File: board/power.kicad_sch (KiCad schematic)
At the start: 22 parts, among them Q1 BSS138, Q2 BSS138, Q3 BSS138, U1 OKI-78SR-5_1.5-W36H-C

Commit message: assigned footprints
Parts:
- C1, C2: footprint (none) -> Capacitor_SMD:C_0603_1608Metric_Pad1.08x0.95mm_HandSolder
- Conn1, Conn11, Conn14, Conn15: footprint (none) -> MRDT_Connectors:Square_Anderson_2_H_Side_By_Side_PV
- D1, D2, D3, D4, D5, D6: footprint (none) -> LED_SMD:LED_0603_1608Metric_Pad1.05x0.95mm_HandSolder
- R1, R2, R3, R6, R7, R8: footprint (none) -> Resistor_SMD:R_0603_1608Metric_Pad0.98x0.95mm_HandSolder
- U1: footprint Converter_DCDC:Converter_DCDC_Murata_OKI-78SR_Horizontal -> MRDT_Devices:OKI_Horizontal
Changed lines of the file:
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@@
 			)
 		)
-		(property "Footprint" ""
+		(property "Footprint" "LED_SMD:LED_0603_1608Metric_Pad1.05x0.95mm_HandSolder"
 			(at 87.63 100.33 0)
 			(effects
@@
 			)
 		)
-		(property "Footprint" ""
+		(property "Footprint" "LED_SMD:LED_0603_1608Metric_Pad1.05x0.95mm_HandSolder"
 			(at 168.91 48.26 0)
 			(effects
@@
 			)
 		)
-		(property "Footprint" ""
+		(property "Footprint" "Capacitor_SMD:C_0603_1608Metric_Pad1.08x0.95mm_HandSolder"
 			(at 93.6752 49.53 0)
 			(effects
@@
 			)
 		)
-		(property "Footprint" ""
+		(property "Footprint" "MRDT_Connectors:Square_Anderson_2_H_Side_By_Side_PV"
 			(at 26.67 114.3 0)
 			(effects
@@
 			)
 		)
-		(property "Footprint" ""
+		(property "Footprint" "MRDT_Connectors:Square_Anderson_2_H_Side_By_Side_PV"
 			(at 25.4 60.96 0)
 			(effects
@@
 			)
 		)
-		(property "Footprint" "Converter_DCDC:Converter_DCDC_Murata_OKI-78SR_Horizontal"
+		(property "Footprint" "MRDT_Devices:OKI_Horizontal"
 			(at 109.22 45.72 0)
 			(effects
@@
 			)
 		)
-		(property "Footprint" ""
+		(property "Footprint" "MRDT_Connectors:Square_Anderson_2_H_Side_By_Side_PV"
 			(at 26.67 201.93 0)
 			(effects
@@
 			)
 		)
-		(property "Footprint" ""
+		(property "Footprint" "MRDT_Connectors:Square_Anderson_2_H_Side_By_Side_PV"
 			(at 25.4 49.53 0)
 			(effects
@@
 			)
 		)
-		(property "Footprint" ""
+		(property "Footprint" "MRDT_Connectors:Square_Anderson_2_H_Side_By_Side_PV"
 			(at 26.67 143.51 0)
 			(effects
@@
 			)
 		)
-		(property "Footprint" ""
+		(property "Footprint" "LED_SMD:LED_0603_1608Metric_Pad1.05x0.95mm_HandSolder"
 			(at 163.83 100.33 0)
 			(effects
@@
 			)
 		)
-		(property "Footprint" ""
+		(property "Footprint" "MRDT_Connectors:Square_Anderson_2_H_Side_By_Side_PV"
 			(at 26.67 99.06 0)
 			(effects
@@
 			)
 		)
-		(property "Footprint" ""
+		(property "Footprint" "Resistor_SMD:R_0603_1608Metric_Pad0.98x0.95mm_HandSolder"
 			(at 157.226 39.624 90)
 			(effects
@@
 			)
 		)
-		(property "Footprint" ""
+		(property "Footprint" "MRDT_Connectors:Square_Anderson_2_H_Side_By_Side_PV"
 			(at 26.67 158.75 0)
 			(effects
@@
 			)
 		)
-		(property "Footprint" ""
+		(property "Footprint" "MRDT_Connectors:Square_Anderson_2_H_Side_By_Side_PV"
 			(at 26.67 186.69 0)
 			(effects
@@
 			)
 		)
-		(property "Footprint" ""
+		(property "Footprint" "Resistor_SMD:R_0603_1608Metric_Pad0.98x0.95mm_HandSolder"
 			(at 144.526 39.624 90)
 			(effects
@@
 			)
 		)
-		(property "Footprint" ""
+		(property "Footprint" "Resistor_SMD:R_0603_1608Metric_Pad0.98x0.95mm_HandSolder"
 			(at 125.476 91.694 90)
 			(effects
@@
 			)
 		)
-		(property "Footprint" ""
+		(property "Footprint" "Capacitor_SMD:C_0603_1608Metric_Pad1.08x0.95mm_HandSolder"
 			(at 124.1552 50.8 0)
 			(effects
@@
 			)
 		)
-		(property "Footprint" ""
+		(property "Footprint" "LED_SMD:LED_0603_1608Metric_Pad1.05x0.95mm_HandSolder"
 			(at 143.51 48.26 0)
 			(effects
@@
 			)
 		)
-		(property "Footprint" ""
+		(property "Footprint" "Resistor_SMD:R_0603_1608Metric_Pad0.98x0.95mm_HandSolder"
 			(at 88.646 91.694 90)
 			(effects
@@
 			)
 		)
-		(property "Footprint" ""
+		(property "Footprint" "Resistor_SMD:R_0603_1608Metric_Pad0.98x0.95mm_HandSolder"
 			(at 164.846 91.694 90)
 			(effects
@@
 			)
 		)
-		(property "Footprint" ""
+		(property "Footprint" "LED_SMD:LED_0603_1608Metric_Pad1.05x0.95mm_HandSolder"
 			(at 124.46 100.33 0)
 			(effects
@@
 			)
 		)
-		(property "Footprint" ""
+		(property "Footprint" "Resistor_SMD:R_0603_1608Metric_Pad0.98x0.95mm_HandSolder"
 			(at 169.926 39.624 90)
 			(effects
@@
 			)
 		)
-		(property "Footprint" ""
+		(property "Footprint" "LED_SMD:LED_0603_1608Metric_Pad1.05x0.95mm_HandSolder"
 			(at 156.21 48.26 0)
 			(effects

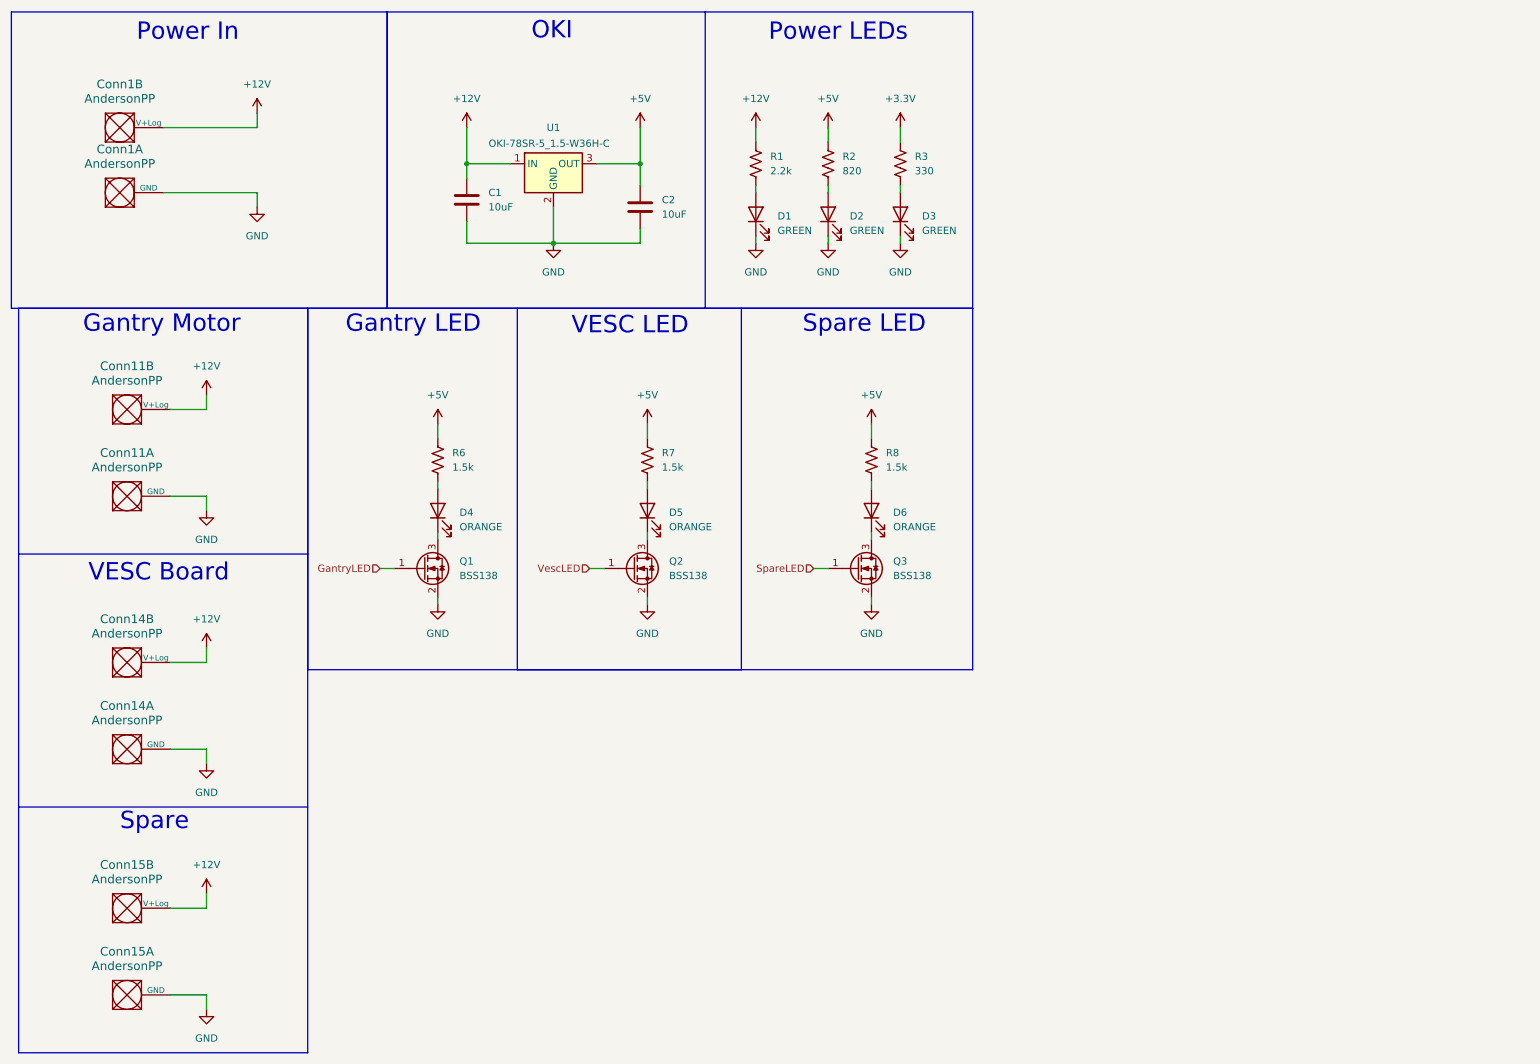
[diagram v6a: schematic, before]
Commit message: Fixed issues after schematic review
added 6 leds for every servo, changed txd and rxd to pins 30/31, added additional oki for 3.3V
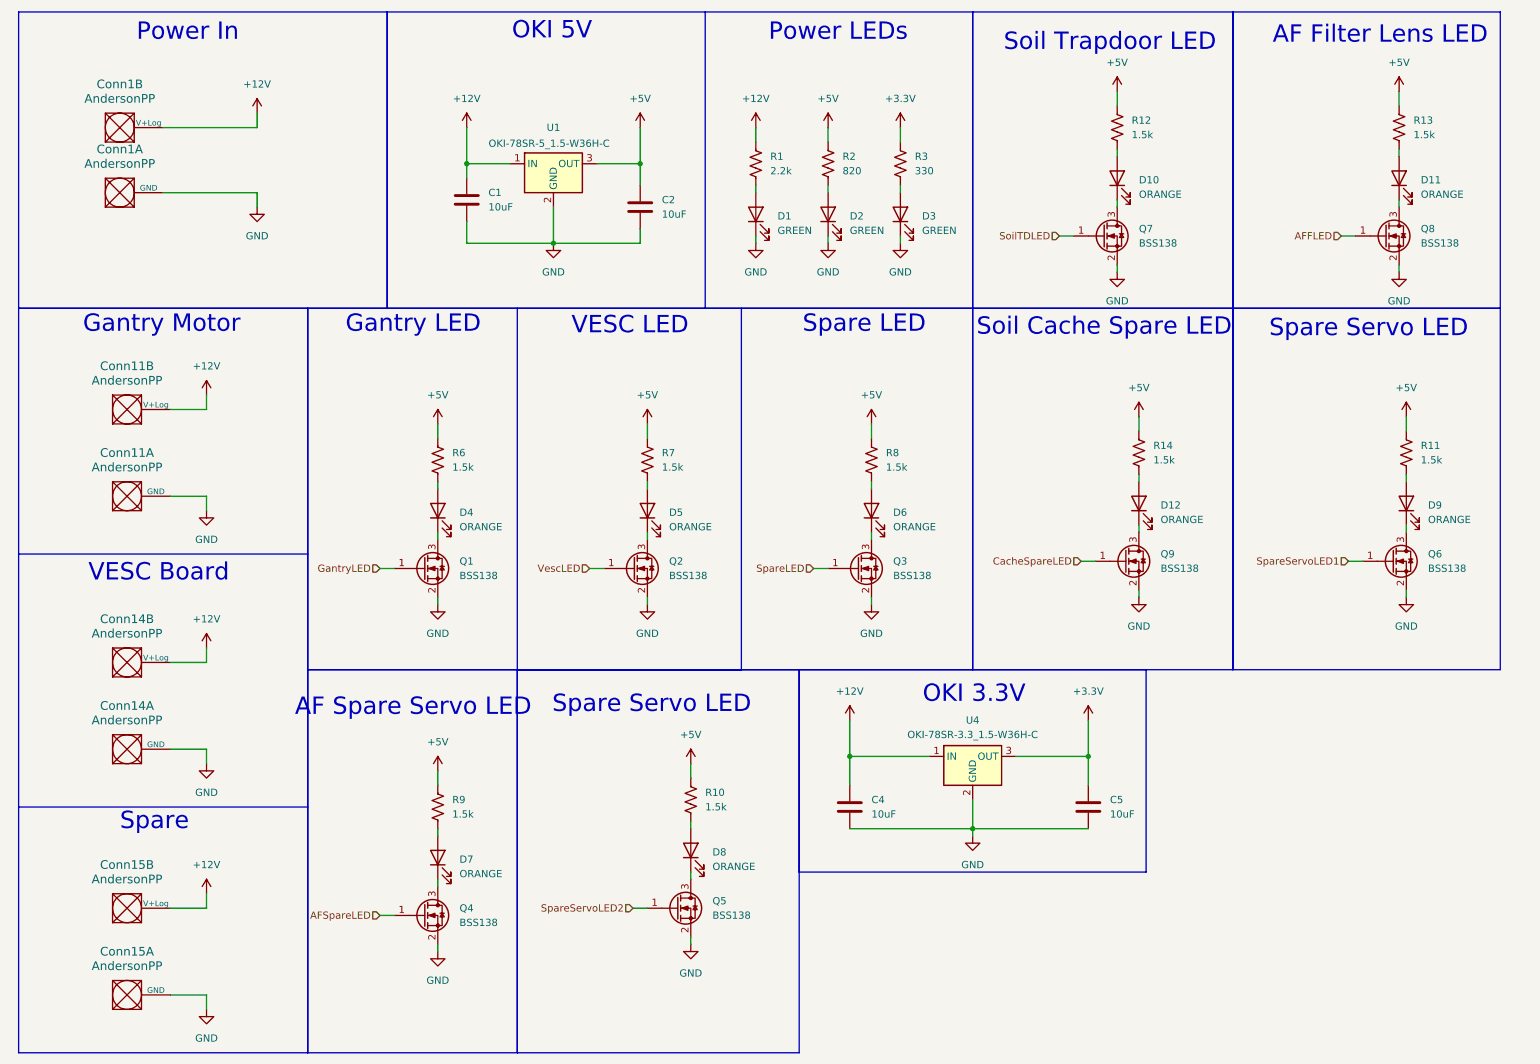
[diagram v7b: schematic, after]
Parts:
- added C4, C5: 10uF, symbol Device:C
- added D10, D11, D12, D7, D8, D9: ORANGE, LED_SMD:LED_0603_1608Metric_Pad1.05x0.95mm_HandSolder, symbol Device:LED
- added Q4, Q5, Q6, Q7, Q8, Q9: BSS138, Package_TO_SOT_SMD:SOT-23, symbol Transistor_FET:BSS138
- added R10, R11, R12, R13, R14, R9: 1.5k, Resistor_SMD:R_0603_1608Metric_Pad0.98x0.95mm_HandSolder, symbol Device:R_US
- added U4: OKI-78SR-3.3_1.5-W36H-C, Converter_DCDC:Converter_DCDC_Murata_OKI-78SR_Horizontal, symbol Converter_DCDC:OKI-78SR-3.3_1.5-W36H-C
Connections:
- net +12V: now also C4.1, U4.1 (IN)
- net +3.3V: now also C5.1, U4.3 (OUT)
- net +5V: now also R10.1, R11.1, R12.1, R13.1, R14.1, R9.1
- net GND: now also C4.2, C5.2, Q4.2 (S), Q5.2 (S), Q6.2 (S), Q7.2 (S), Q8.2 (S), Q9.2 (S), U4.2 (GND)
- new net: D7.2 (A), R9.2
- new net: D9.1 (K), Q6.3 (D)
- new net: D10.2 (A), R12.2
- new net: D10.1 (K), Q7.3 (D)
- new net: D11.2 (A), R13.2
- new net: D8.1 (K), Q5.3 (D)
- new net: D9.2 (A), R11.2
- new net: D12.1 (K), Q9.3 (D)
- new net: D12.2 (A), R14.2
- new net: D7.1 (K), Q4.3 (D)
- new net: D8.2 (A), R10.2
- new net: D11.1 (K), Q8.3 (D)
- new net AFFLED: Q8.1 (G)
- new net AFSpareLED: Q4.1 (G)
- new net CacheSpareLED: Q9.1 (G)
- new net SoilTDLED: Q7.1 (G)
- new net SpareServoLED1: Q6.1 (G)
- new net SpareServoLED2: Q5.1 (G)
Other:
- note added: "AF Filter Lens LED"
- note added: "AF Spare Servo LED"
- note added: "OKI 3.3V"
- note added: "OKI 5V"
- note added: "Soil Cache Spare LED"
- note added: "Soil Trapdoor LED"
- note added: "Spare Servo LED"
- note removed: "OKI"

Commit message: Edited names and locations for readability
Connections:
- net SpareLED renamed SpareMotorLED
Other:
- note added: "Spare Motor LED"
- note removed: "Spare LED"
- moved on the sheet: C4, C5, D1, D2, D3, D6, Q3, R1, R2, R3, R8, U4
